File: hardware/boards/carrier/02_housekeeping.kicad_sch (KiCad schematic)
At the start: 13 parts, among them SW1 SKSCLCE010, U1 STM32C092GCU7

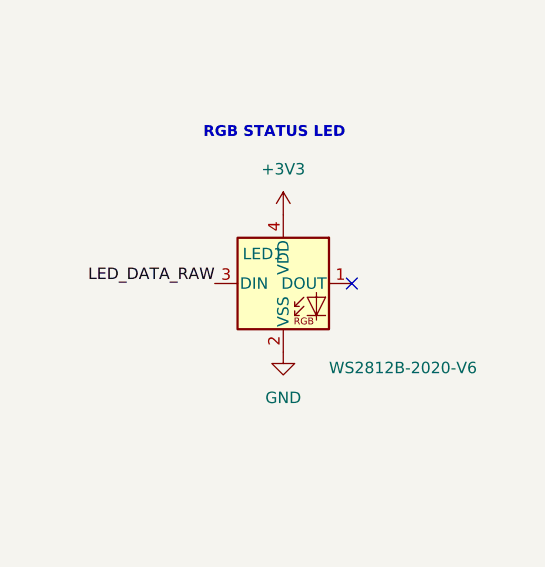
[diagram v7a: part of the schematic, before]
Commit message: Add carrier status LED bypass capacitor
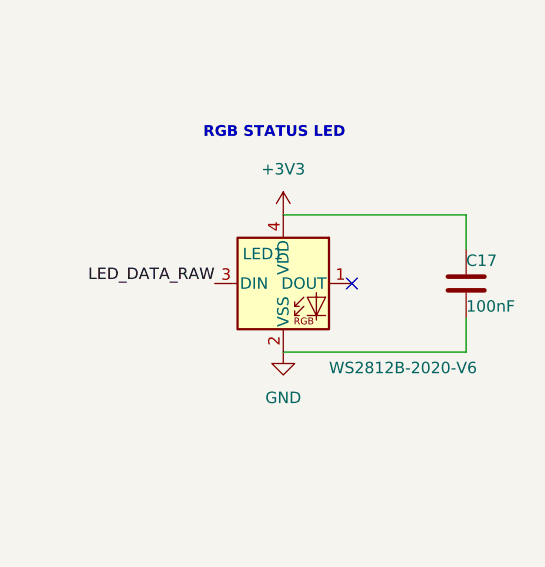
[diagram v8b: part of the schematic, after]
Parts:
- added C17: 100nF, Capacitor_SMD:C_0603_1608Metric, symbol Device:C
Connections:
- net +3V3: now also C17.1
- net GND: now also C17.2
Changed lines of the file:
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@@
+	(wire
+		(pts
+			(xy 359.41 109.22) (xy 359.41 105.41)
+		)
+		(stroke
+			(width 0)
+			(type default)
+		)
+	)
+	(wire
+		(pts
+			(xy 339.09 105.41) (xy 359.41 105.41)
+		)
+		(stroke
+			(width 0)
+			(type default)
+		)
+	)
+	(wire
+		(pts
+			(xy 359.41 116.84) (xy 359.41 120.65)
+		)
+		(stroke
+			(width 0)
+			(type default)
+		)
+	)
+	(wire
+		(pts
+			(xy 339.09 120.65) (xy 359.41 120.65)
+		)
+		(stroke
+			(width 0)
+			(type default)
+		)
+	)
 	(wire
 		(pts
@@
 					(unit 1)
 				)
+			)
+		)
+	)
+	(symbol
+		(lib_id "Device:C")
+		(at 359.41 113.03 0)
+		(unit 1)
+		(body_style 1)
+		(exclude_from_sim no)
+		(in_bom yes)
+		(on_board yes)
+		(in_pos_files yes)
+		(dnp no)
+		(property "Reference" "C17"
+			(at 359.41 110.49 0)
+			(show_name no)
+			(do_not_autoplace no)
+			(effects
+				(font
+					(size 1.27 1.27)
+				)
+				(justify left)
+			)
+		)
+		(property "Value" "100nF"
+			(at 359.41 115.57 0)
+			(show_name no)
+			(do_not_autoplace no)
+			(effects
+				(font
+					(size 1.27 1.27)
+				)
+				(justify left)
+			)
+		)
+		(property "Footprint" "Capacitor_SMD:C_0603_1608Metric"
+			(at 360.375 109.22 0)
+			(hide yes)
+			(show_name no)
+			(do_not_autoplace no)
+			(effects
+				(font
+					(size 1.27 1.27)
+				)
+			)
+		)
+		(property "Datasheet" ""
+			(at 359.41 113.03 0)
+			(hide yes)
+			(show_name no)
+			(do_not_autoplace no)
+			(effects
+				(font
+					(size 1.27 1.27)
+				)
+			)
+		)
+		(property "Description" "LED local bypass capacitor"
+			(at 359.41 113.03 0)
+			(hide yes)
+			(show_name no)
+			(do_not_autoplace no)
+			(effects
+				(font
+					(size 1.27 1.27)
+				)
+			)
+		)
+		(pin "1"
+		)
+		(pin "2"
+		)
+		(instances
+			(project "carrier"
+				(path "/ee42a069-09cc-4091-bee3-2dd6ab96c98c/64ed744c-f0e1-4d20-9137-f6a463447101"
+					(reference "C17")
+					(unit 1)
+				)
